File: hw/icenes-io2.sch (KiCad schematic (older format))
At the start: 12 parts

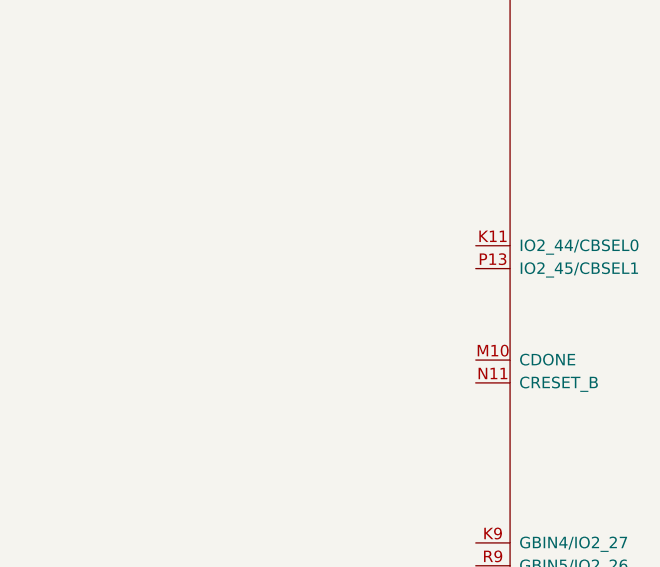
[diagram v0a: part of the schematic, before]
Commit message: Added voltage generators for 3.3V, 1.2V and 5V. Added more info and footprints to some components. Connected signals to the NES connector to banks 0 and 1.
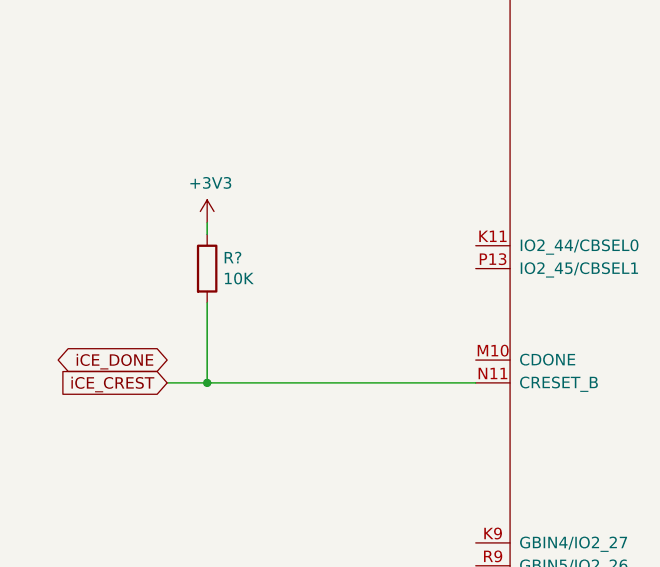
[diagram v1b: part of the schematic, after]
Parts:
- added R?: R10K, Resistor_SMD:R_0603_1608Metric_Pad1.05x0.95mm_HandSolder, symbol icenes-library:R10K
- C? (x9): footprint (none) -> Capacitor_SMD:C_0603_1608Metric_Pad1.05x0.95mm_HandSolder; Manufacturer (none) -> Wurth; Part number (none) -> 885012206020
- C?: footprint (none) -> Capacitor_SMD:C_0603_1608Metric_Pad1.05x0.95mm_HandSolder; Manufacturer (none) -> Murata; Part number (none) -> GRM188R61A106KE69D
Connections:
- net +3V3: now also R?.1
- net iCE_CREST: now reaches U?.N11 (CRESET_B)
- net iCE_CREST: now also R?.2
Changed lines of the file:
@@
 F 0 "C?" H 4165 2396 50  0000 L CNN
 F 1 "C0.1uF" H 3900 2250 50  0001 C CNN
-F 2 "" H 4050 2350 50  0001 C CNN
+F 2 "Capacitor_SMD:C_0603_1608Metric_Pad1.05x0.95mm_HandSolder" H 4050 2350 50  0001 C CNN
 F 3 "" H 4050 2350 50  0001 C CNN
 F 4 "0.1uF" H 4165 2305 50  0000 L CNN "Capacitance"
+F 5 "Wurth" H 4050 2350 50  0001 C CNN "Manufacturer"
+F 6 "885012206020 " H 4050 2350 50  0001 C CNN "Part number"
 	1    4050 2350
 	1    0    0    -1
@@
 F 0 "C?" H 3715 2396 50  0000 L CNN
 F 1 "C0.1uF" H 3450 2250 50  0001 C CNN
-F 2 "" H 3600 2350 50  0001 C CNN
+F 2 "Capacitor_SMD:C_0603_1608Metric_Pad1.05x0.95mm_HandSolder" H 3600 2350 50  0001 C CNN
 F 3 "" H 3600 2350 50  0001 C CNN
 F 4 "0.1uF" H 3715 2305 50  0000 L CNN "Capacitance"
+F 5 "Wurth" H 3600 2350 50  0001 C CNN "Manufacturer"
+F 6 "885012206020 " H 3600 2350 50  0001 C CNN "Part number"
 	1    3600 2350
 	1    0    0    -1
@@
 F 0 "C?" H 3265 2396 50  0000 L CNN
 F 1 "C0.1uF" H 3000 2250 50  0001 C CNN
-F 2 "" H 3150 2350 50  0001 C CNN
+F 2 "Capacitor_SMD:C_0603_1608Metric_Pad1.05x0.95mm_HandSolder" H 3150 2350 50  0001 C CNN
 F 3 "" H 3150 2350 50  0001 C CNN
 F 4 "0.1uF" H 3265 2305 50  0000 L CNN "Capacitance"
+F 5 "Wurth" H 3150 2350 50  0001 C CNN "Manufacturer"
+F 6 "885012206020 " H 3150 2350 50  0001 C CNN "Part number"
 	1    3150 2350
 	1    0    0    -1
@@
 F 0 "C?" H 2815 2396 50  0000 L CNN
 F 1 "C0.1uF" H 2550 2250 50  0001 C CNN
-F 2 "" H 2700 2350 50  0001 C CNN
+F 2 "Capacitor_SMD:C_0603_1608Metric_Pad1.05x0.95mm_HandSolder" H 2700 2350 50  0001 C CNN
 F 3 "" H 2700 2350 50  0001 C CNN
 F 4 "0.1uF" H 2815 2305 50  0000 L CNN "Capacitance"
+F 5 "Wurth" H 2700 2350 50  0001 C CNN "Manufacturer"
+F 6 "885012206020 " H 2700 2350 50  0001 C CNN "Part number"
 	1    2700 2350
 	1    0    0    -1
@@
 F 0 "C?" H 11115 2446 50  0000 L CNN
 F 1 "C0.1uF" H 10850 2300 50  0001 C CNN
-F 2 "" H 11000 2400 50  0001 C CNN
+F 2 "Capacitor_SMD:C_0603_1608Metric_Pad1.05x0.95mm_HandSolder" H 11000 2400 50  0001 C CNN
 F 3 "" H 11000 2400 50  0001 C CNN
 F 4 "0.1uF" H 11115 2355 50  0000 L CNN "Capacitance"
+F 5 "Wurth" H 11000 2400 50  0001 C CNN "Manufacturer"
+F 6 "885012206020 " H 11000 2400 50  0001 C CNN "Part number"
 	1    11000 2400
 	1    0    0    -1
@@
 F 0 "C?" H 10665 2446 50  0000 L CNN
 F 1 "C0.1uF" H 10400 2300 50  0001 C CNN
-F 2 "" H 10550 2400 50  0001 C CNN
+F 2 "Capacitor_SMD:C_0603_1608Metric_Pad1.05x0.95mm_HandSolder" H 10550 2400 50  0001 C CNN
 F 3 "" H 10550 2400 50  0001 C CNN
 F 4 "0.1uF" H 10665 2355 50  0000 L CNN "Capacitance"
+F 5 "Wurth" H 10550 2400 50  0001 C CNN "Manufacturer"
+F 6 "885012206020 " H 10550 2400 50  0001 C CNN "Part number"
 	1    10550 2400
 	1    0    0    -1
@@
 F 0 "C?" H 10215 2446 50  0000 L CNN
 F 1 "C0.1uF" H 9950 2300 50  0001 C CNN
-F 2 "" H 10100 2400 50  0001 C CNN
+F 2 "Capacitor_SMD:C_0603_1608Metric_Pad1.05x0.95mm_HandSolder" H 10100 2400 50  0001 C CNN
 F 3 "" H 10100 2400 50  0001 C CNN
 F 4 "0.1uF" H 10215 2355 50  0000 L CNN "Capacitance"
+F 5 "Wurth" H 10100 2400 50  0001 C CNN "Manufacturer"
+F 6 "885012206020 " H 10100 2400 50  0001 C CNN "Part number"
 	1    10100 2400
 	1    0    0    -1
@@
 F 0 "C?" H 9765 2446 50  0000 L CNN
 F 1 "C0.1uF" H 9500 2300 50  0001 C CNN
-F 2 "" H 9650 2400 50  0001 C CNN
+F 2 "Capacitor_SMD:C_0603_1608Metric_Pad1.05x0.95mm_HandSolder" H 9650 2400 50  0001 C CNN
 F 3 "" H 9650 2400 50  0001 C CNN
 F 4 "0.1uF" H 9765 2355 50  0000 L CNN "Capacitance"
+F 5 "Wurth" H 9650 2400 50  0001 C CNN "Manufacturer"
+F 6 "885012206020 " H 9650 2400 50  0001 C CNN "Part number"
 	1    9650 2400
 	1    0    0    -1
@@
 F 0 "C?" H 4165 3596 50  0000 L CNN
 F 1 "C0.1uF" H 3900 3450 50  0001 C CNN
-F 2 "" H 4050 3550 50  0001 C CNN
+F 2 "Capacitor_SMD:C_0603_1608Metric_Pad1.05x0.95mm_HandSolder" H 4050 3550 50  0001 C CNN
 F 3 "" H 4050 3550 50  0001 C CNN
 F 4 "0.1uF" H 4165 3505 50  0000 L CNN "Capacitance"
+F 5 "Wurth" H 4050 3550 50  0001 C CNN "Manufacturer"
+F 6 "885012206020 " H 4050 3550 50  0001 C CNN "Part number"
 	1    4050 3550
 	1    0    0    -1
@@
 AR Path="/5D1BB1FB/5D33E08F" Ref="C?"  Part="1"
 AR Path="/5D1BB49B/5D33E08F" Ref="C?"  Part="1"
+AR Path="/5D33E08F" Ref="C?"  Part="1"
 F 0 "C?" H 3715 3596 50  0000 L CNN
 F 1 "C10uF" H 3450 3450 50  0001 C CNN
-F 2 "" V 3600 3550 50  0001 C CNN
+F 2 "Capacitor_SMD:C_0603_1608Metric_Pad1.05x0.95mm_HandSolder" V 3600 3550 50  0001 C CNN
 F 3 "" H 3600 3550 50  0001 C CNN
 F 4 "10uF" H 3715 3505 50  0000 L CNN "Capacitance"
+F 5 "Murata" H 3600 3550 50  0001 C CNN "Manufacturer"
+F 6 "GRM188R61A106KE69D " H 3600 3550 50  0001 C CNN "Part number"
 	1    3600 3550
 	1    0    0    -1
@@
 Wire Wire Line
 	4550 3450 4550 3750
+$Comp
+L power:+3V3 #PWR?
+U 1 1 5D1F4C80
+P 3425 4750
+AR Path="/5D1BB1FB/5D1F4C80" Ref="#PWR?"  Part="1"
+AR Path="/5D1BB49B/5D1F4C80" Ref="#PWR?"  Part="1"
+F 0 "#PWR?" H 3425 4600 50  0001 C CNN
+F 1 "+3V3" H 3440 4923 50  0000 C CNN
+F 2 "" H 3425 4750 50  0001 C CNN
+F 3 "" H 3425 4750 50  0001 C CNN
+	1    3425 4750
+	1    0    0    -1
+$EndComp
+$Comp
+L icenes-library:R10K R?
+U 1 1 5D1F5A80
+P 3425 4950
+F 0 "R?" V 3379 5020 50  0000 L CNN
+F 1 "R10K" H 3425 4850 50  0001 C CNN
+F 2 "Resistor_SMD:R_0603_1608Metric_Pad1.05x0.95mm_HandSolder" V 3425 4950 50  0001 C CNN
+F 3 "" V 3425 4950 50  0001 C CNN
+F 4 "10K" V 3470 5020 50  0000 L CNN "Resistance"
+F 5 "Yageo" H 3425 4950 50  0001 C CNN "Manufacturer"
+F 6 "RC0603FR-0710KL" H 3425 4950 50  0001 C CNN "Part number"
+	1    3425 4950
+	0    1    1    0
+$EndComp
+Text GLabel 3250 5450 0    50   Input ~ 0
+iCE_CREST
+Wire Wire Line
+	4600 5450 3425 5450
+Connection ~ 3425 5450
+Wire Wire Line
+	3425 5450 3250 5450
+Wire Wire Line
+	3425 4800 3425 4750
+Text GLabel 3250 5350 0    50   BiDi ~ 0
+iCE_DONE
+Wire Wire Line
+	3425 5100 3425 5450
 $EndSCHEMATC

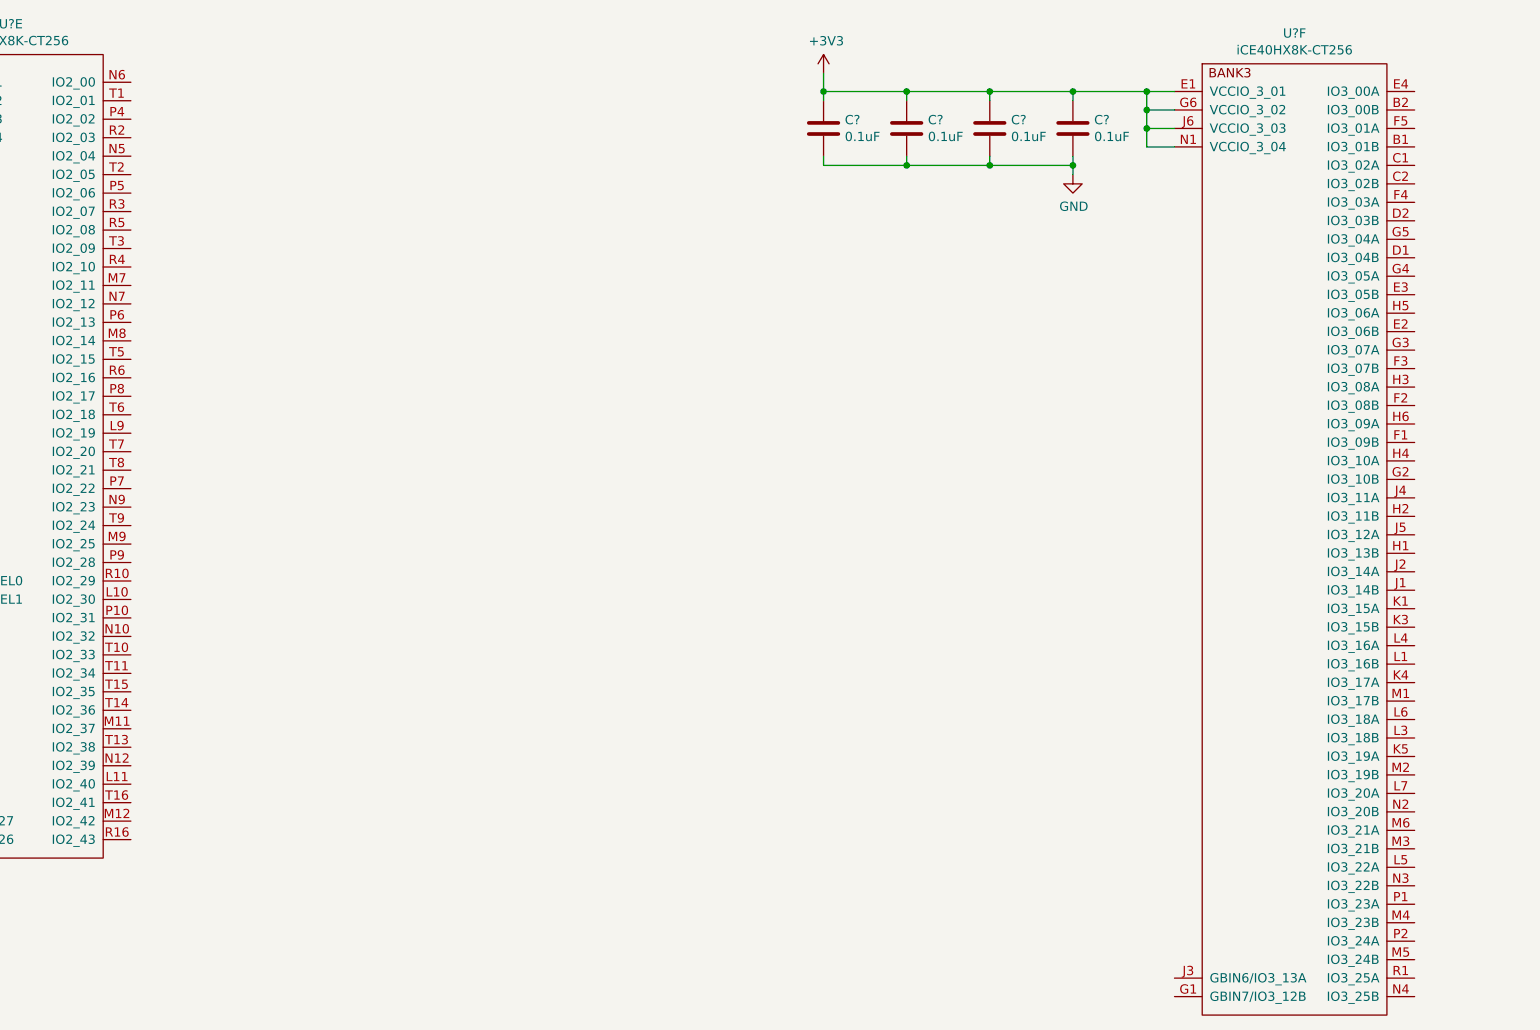
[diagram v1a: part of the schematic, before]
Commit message: Added 8 LED. Added GPIO header for the rest of the GPIO pins on bank1. Labeled all GPIO pins.
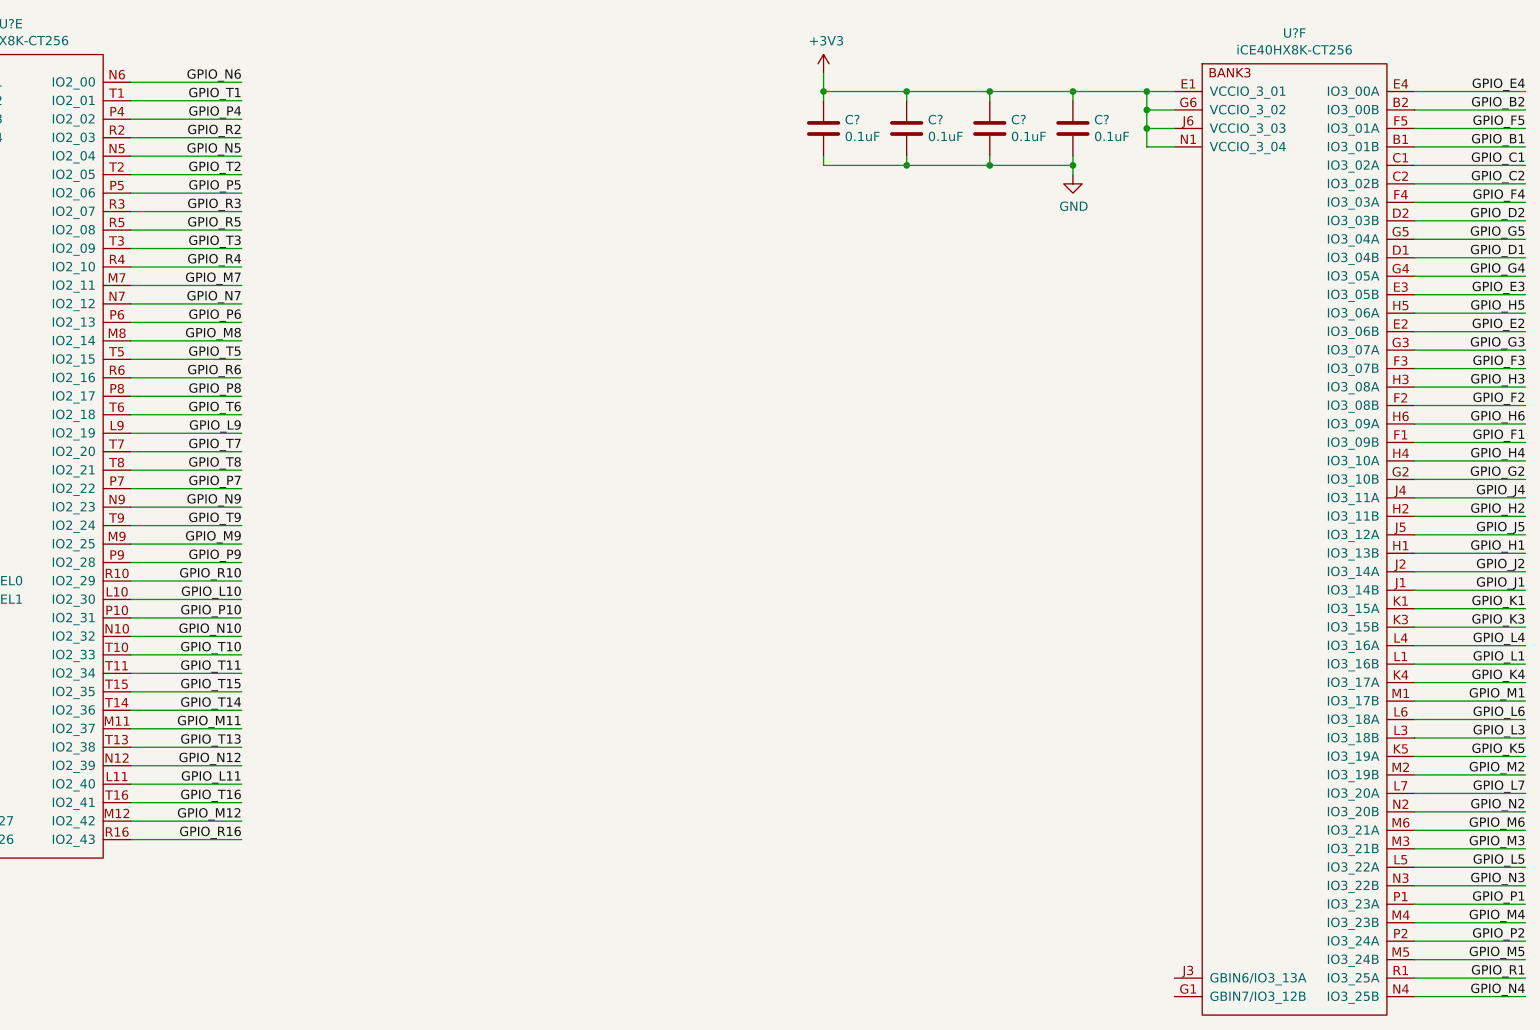
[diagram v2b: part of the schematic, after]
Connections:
- net GPIO_L10: now reaches U?.L10 (IO2_30)
- net GPIO_L11: now reaches U?.L11 (IO2_40)
- net GPIO_L9: now reaches U?.L9 (IO2_19)
- net GPIO_M11: now reaches U?.M11 (IO2_37)
- net GPIO_M12: now reaches U?.M12 (IO2_42)
- net GPIO_M7: now reaches U?.M7 (IO2_11)
- net GPIO_M8: now reaches U?.M8 (IO2_14)
- net GPIO_M9: now reaches U?.M9 (IO2_25)
- net GPIO_N10: now reaches U?.N10 (IO2_32)
- net GPIO_N12: now reaches U?.N12 (IO2_39)
- net GPIO_N5: now reaches U?.N5 (IO2_04)
- net GPIO_N6: now reaches U?.N6 (IO2_00)
- net GPIO_N7: now reaches U?.N7 (IO2_12)
- net GPIO_N9: now reaches U?.N9 (IO2_23)
- net GPIO_P10: now reaches U?.P10 (IO2_31)
- net GPIO_P4: now reaches U?.P4 (IO2_02)
- net GPIO_P5: now reaches U?.P5 (IO2_06)
- net GPIO_P6: now reaches U?.P6 (IO2_13)
- net GPIO_P7: now reaches U?.P7 (IO2_22)
- net GPIO_P8: now reaches U?.P8 (IO2_17)
- net GPIO_P9: now reaches U?.P9 (IO2_28)
- net GPIO_R10: now reaches U?.R10 (IO2_29)
- net GPIO_R16: now reaches U?.R16 (IO2_43)
- net GPIO_R2: now reaches U?.R2 (IO2_03)
- net GPIO_R3: now reaches U?.R3 (IO2_07)
- net GPIO_R4: now reaches U?.R4 (IO2_10)
- net GPIO_R5: now reaches U?.R5 (IO2_08)
- net GPIO_R6: now reaches U?.R6 (IO2_16)
- net GPIO_T1: now reaches U?.T1 (IO2_01)
- net GPIO_T10: now reaches U?.T10 (IO2_33)
- net GPIO_T11: now reaches U?.T11 (IO2_34)
- net GPIO_T13: now reaches U?.T13 (IO2_38)
- net GPIO_T14: now reaches U?.T14 (IO2_36)
- net GPIO_T15: now reaches U?.T15 (IO2_35)
- net GPIO_T16: now reaches U?.T16 (IO2_41)
- net GPIO_T2: now reaches U?.T2 (IO2_05)
- net GPIO_T3: now reaches U?.T3 (IO2_09)
- net GPIO_T5: now reaches U?.T5 (IO2_15)
- net GPIO_T6: now reaches U?.T6 (IO2_18)
- net GPIO_T7: now reaches U?.T7 (IO2_20)
- net GPIO_T8: now reaches U?.T8 (IO2_21)
- net GPIO_T9: now reaches U?.T9 (IO2_24)
- net GPIO_B1: now reaches U?.B1 (IO3_01B)
- net GPIO_B2: now reaches U?.B2 (IO3_00B)
- net GPIO_C1: now reaches U?.C1 (IO3_02A)
- net GPIO_C2: now reaches U?.C2 (IO3_02B)
- net GPIO_D1: now reaches U?.D1 (IO3_04B)
- net GPIO_D2: now reaches U?.D2 (IO3_03B)
- net GPIO_E2: now reaches U?.E2 (IO3_06B)
- net GPIO_E3: now reaches U?.E3 (IO3_05B)
- net GPIO_E4: now reaches U?.E4 (IO3_00A)
- net GPIO_F1: now reaches U?.F1 (IO3_09B)
- net GPIO_F2: now reaches U?.F2 (IO3_08B)
- net GPIO_F3: now reaches U?.F3 (IO3_07B)
- net GPIO_F4: now reaches U?.F4 (IO3_03A)
- net GPIO_F5: now reaches U?.F5 (IO3_01A)
- net GPIO_G2: now reaches U?.G2 (IO3_10B)
- net GPIO_G3: now reaches U?.G3 (IO3_07A)
- net GPIO_G4: now reaches U?.G4 (IO3_05A)
- net GPIO_G5: now reaches U?.G5 (IO3_04A)
- net GPIO_H1: now reaches U?.H1 (IO3_13B)
- net GPIO_H2: now reaches U?.H2 (IO3_11B)
- net GPIO_H3: now reaches U?.H3 (IO3_08A)
- net GPIO_H4: now reaches U?.H4 (IO3_10A)
- net GPIO_H5: now reaches U?.H5 (IO3_06A)
- net GPIO_H6: now reaches U?.H6 (IO3_09A)
- net GPIO_J1: now reaches U?.J1 (IO3_14B)
- net GPIO_J2: now reaches U?.J2 (IO3_14A)
- net GPIO_J4: now reaches U?.J4 (IO3_11A)
- net GPIO_J5: now reaches U?.J5 (IO3_12A)
- net GPIO_K1: now reaches U?.K1 (IO3_15A)
- net GPIO_K3: now reaches U?.K3 (IO3_15B)
- net GPIO_K4: now reaches U?.K4 (IO3_17A)
- net GPIO_K5: now reaches U?.K5 (IO3_19A)
- net GPIO_L1: now reaches U?.L1 (IO3_16B)
- net GPIO_L3: now reaches U?.L3 (IO3_18B)
- net GPIO_L4: now reaches U?.L4 (IO3_16A)
- net GPIO_L5: now reaches U?.L5 (IO3_22A)
- net GPIO_L6: now reaches U?.L6 (IO3_18A)
- net GPIO_L7: now reaches U?.L7 (IO3_20A)
- net GPIO_M1: now reaches U?.M1 (IO3_17B)
- net GPIO_M2: now reaches U?.M2 (IO3_19B)
- net GPIO_M3: now reaches U?.M3 (IO3_21B)
- net GPIO_M4: now reaches U?.M4 (IO3_23B)
- net GPIO_M5: now reaches U?.M5 (IO3_24B)
- net GPIO_M6: now reaches U?.M6 (IO3_21A)
- net GPIO_N2: now reaches U?.N2 (IO3_20B)
- net GPIO_N3: now reaches U?.N3 (IO3_22B)
- net GPIO_N4: now reaches U?.N4 (IO3_25B)
- net GPIO_P1: now reaches U?.P1 (IO3_23A)
- net GPIO_P2: now reaches U?.P2 (IO3_24A)
- net GPIO_R1: now reaches U?.R1 (IO3_25A)
